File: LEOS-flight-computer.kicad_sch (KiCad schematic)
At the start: 25 parts, among them J1 MicroFit_1x4, J2 MicroFit_1x4, J3 GPIO, J4 I2C Breakout, J5 SPI Breakout, U1 MCP2562FD, U2 MCP2518FD, U3 SAM-M8Q, Y1 40 MHz

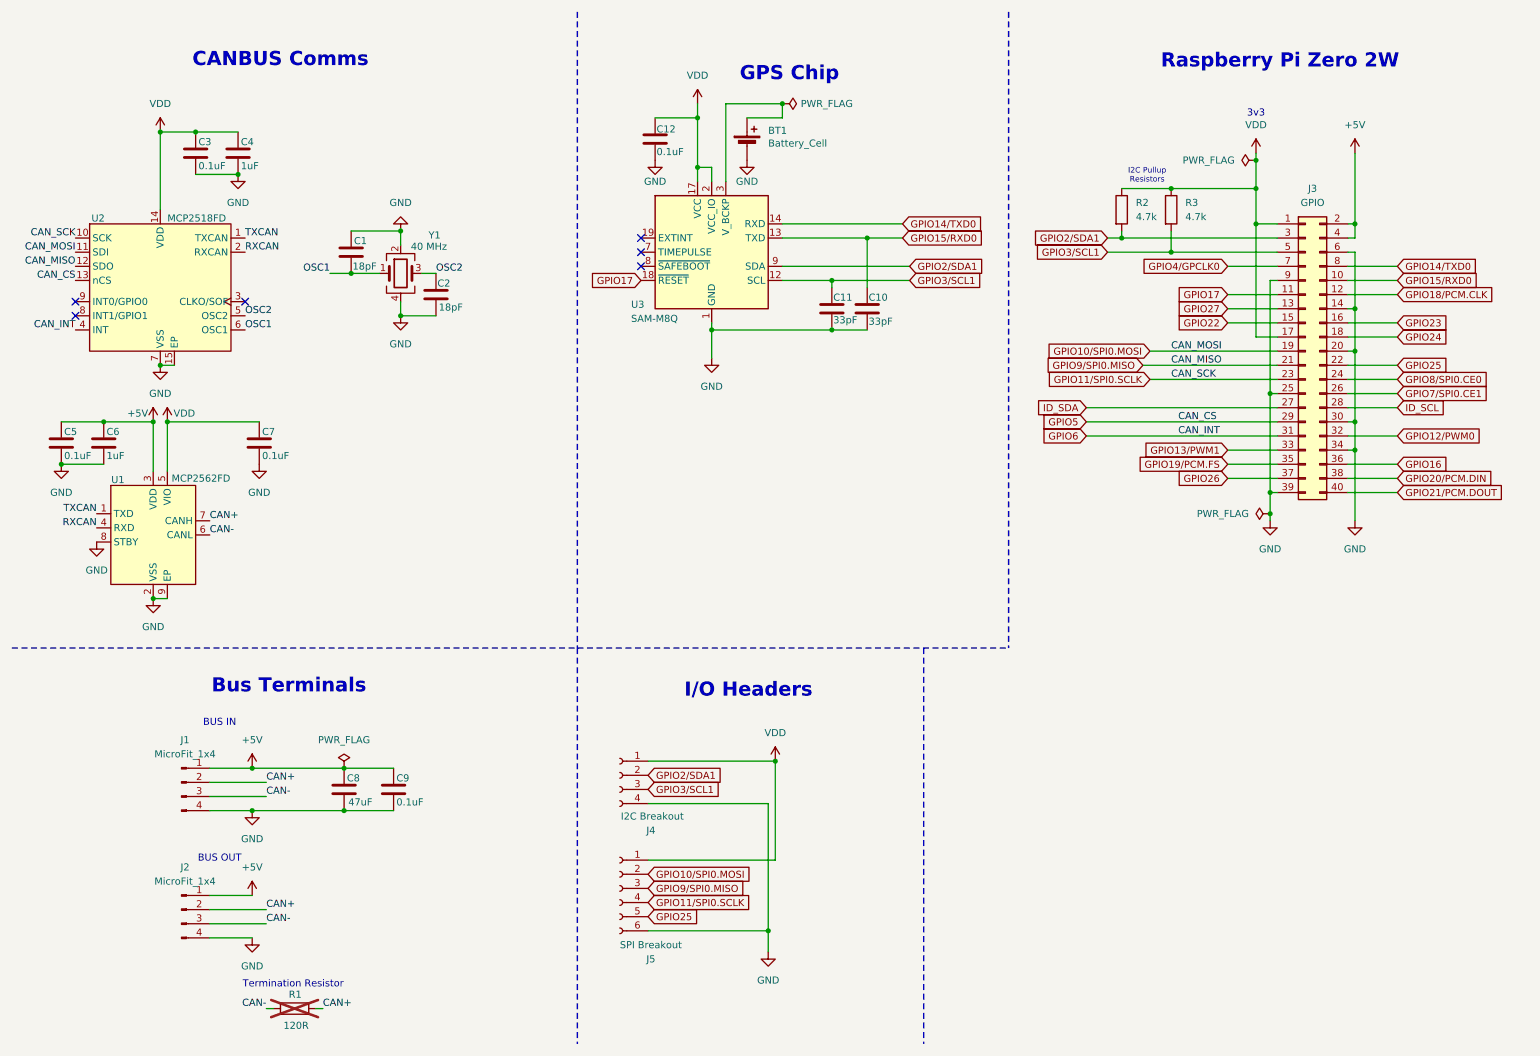
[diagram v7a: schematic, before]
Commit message: v2.1 with redesigned board, connectors, and improved access to RPi
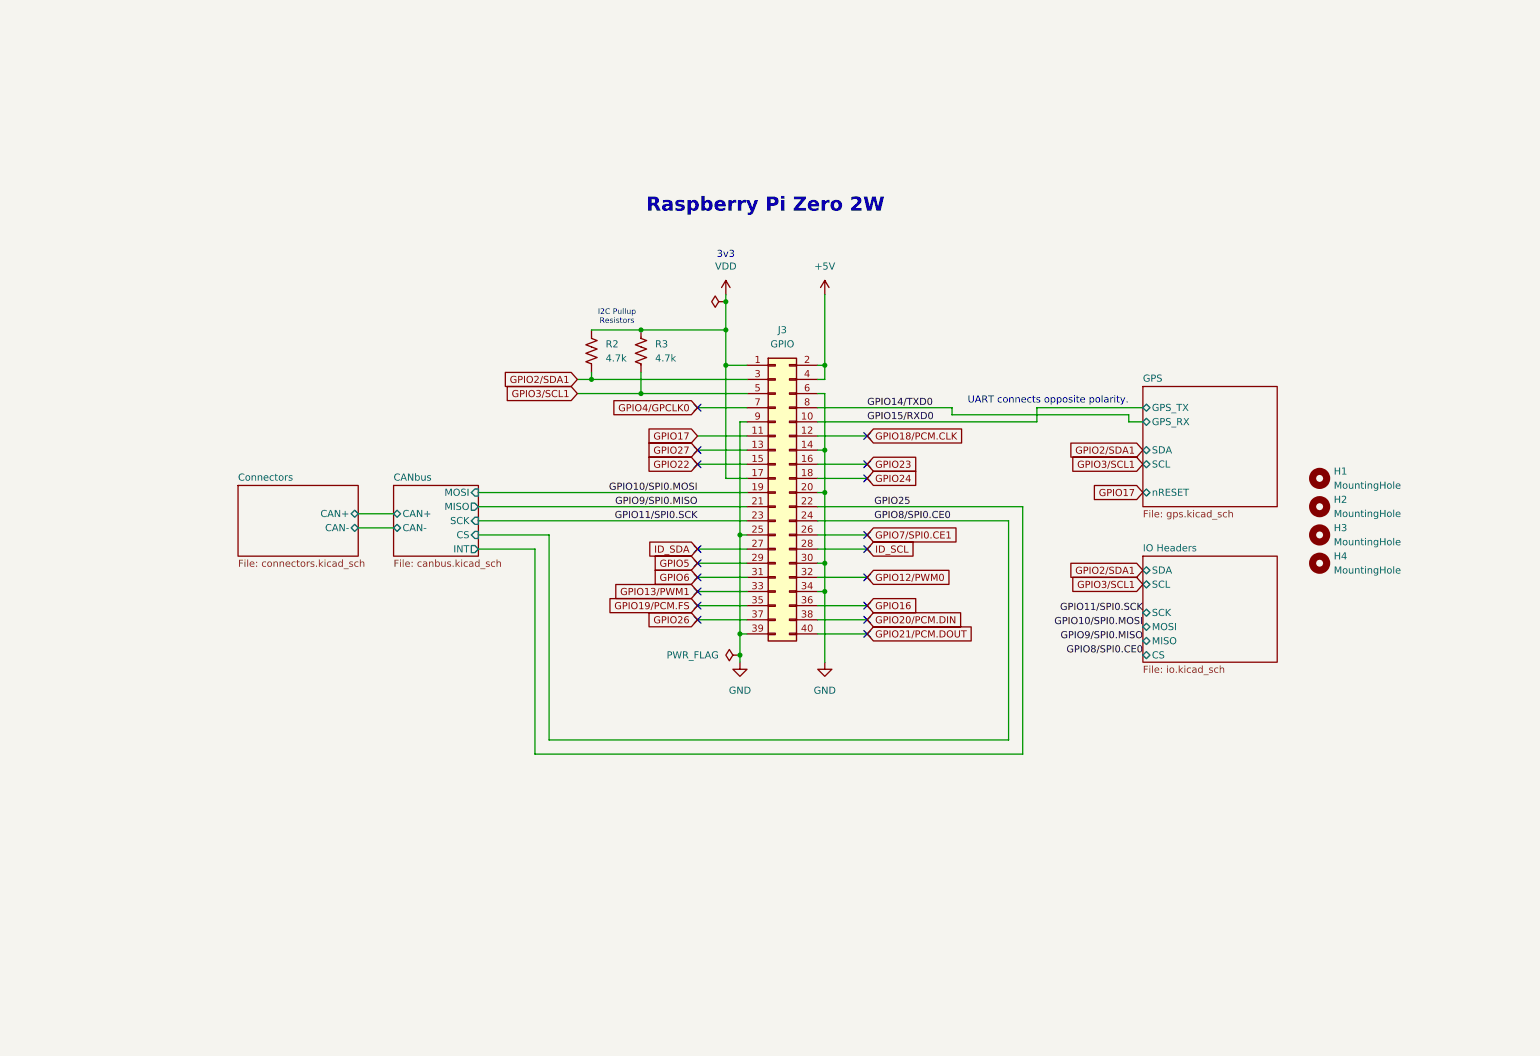
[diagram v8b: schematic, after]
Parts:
- removed BT1: Battery_Cell, CustomFootprints:BatteryHolder_SMD_MYOUNG_BS-08-B2AA010-R, symbol Device:Battery_Cell
- removed C1, C2: 18pF, Capacitor_SMD:C_0603_1608Metric, symbol Device:C
- removed C10, C11: 33pF, Capacitor_SMD:C_0603_1608Metric, symbol Device:C
- removed C12, C3, C5, C7, C9: 0.1uF, Capacitor_SMD:C_0603_1608Metric, symbol Device:C
- removed C4, C6: 1uF, Capacitor_SMD:C_0603_1608Metric, symbol Device:C
- removed C8: 47uF, Capacitor_SMD:C_0603_1608Metric, symbol Device:C
- removed J1, J2: MicroFit_1x4, Connector_Molex:Molex_Micro-Fit_3.0_43650-0410_1x04-1MP_P3.00mm_Horizontal_PnP, symbol Connector:Conn_01x04_Pin
- removed J4: I2C Breakout, Connector_PinSocket_2.54mm:PinSocket_1x04_P2.54mm_Horizontal, symbol Connector:Conn_01x04_Socket
- removed J5: SPI Breakout, Connector_PinSocket_2.54mm:PinSocket_1x06_P2.54mm_Horizontal, symbol Connector:Conn_01x06_Socket
- removed R1: 120R, Resistor_THT:R_Axial_DIN0207_L6.3mm_D2.5mm_P7.62mm_Horizontal, symbol Device:R
- removed R2, R3: 4.7k, Resistor_SMD:R_0603_1608Metric, symbol Device:R
- removed U1: MCP2562FD, Package_SO:SOIC-8_3.9x4.9mm_P1.27mm, symbol LEOS:MCP2562FD
- removed U2: MCP2518FD, Package_SO:SOIC-14_3.9x8.7mm_P1.27mm, symbol LEOS:MCP2518FD
- removed U3: SAM-M8Q, RF_GPS:ublox_SAM-M8Q, symbol RF_GPS:SAM-M8Q
- removed Y1: 40 MHz, Crystal:Crystal_SMD_3225-4Pin_3.2x2.5mm_HandSoldering, symbol Device:Crystal_GND24
- added H1, H2, H3, H4: MountingHole, MountingHole:MountingHole_2.7mm_M2.5, symbol Mechanical:MountingHole
- added R2, R3: 4.7k, Resistor_SMD:R_0603_1608Metric, symbol Device:R_US
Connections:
- net GPIO2/SDA1: now also R2.2
- net GPIO3/SCL1: now also R3.2
- net VDD: now also R2.1, R3.1
- net GPIO11/SPI0.SCLK renamed GPIO11/SPI0.SCK
- no-connect marks 6 -> 18
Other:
- added sheet CANbus (canbus.kicad_sch)
- added sheet Connectors (connectors.kicad_sch)
- added sheet GPS (gps.kicad_sch)
- added sheet IO Headers (io.kicad_sch)
- note added: "UART connects opposite polarity."
- note removed: "BUS IN"
- note removed: "BUS OUT"
- note removed: "Bus Terminals"
- note removed: "CANBUS Comms"
- note removed: "GPS Chip"
- note removed: "I/O Headers"
- note removed: "Termination Resistor"
